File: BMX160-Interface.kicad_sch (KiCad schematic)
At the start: 1 part, among them U1 BMX160

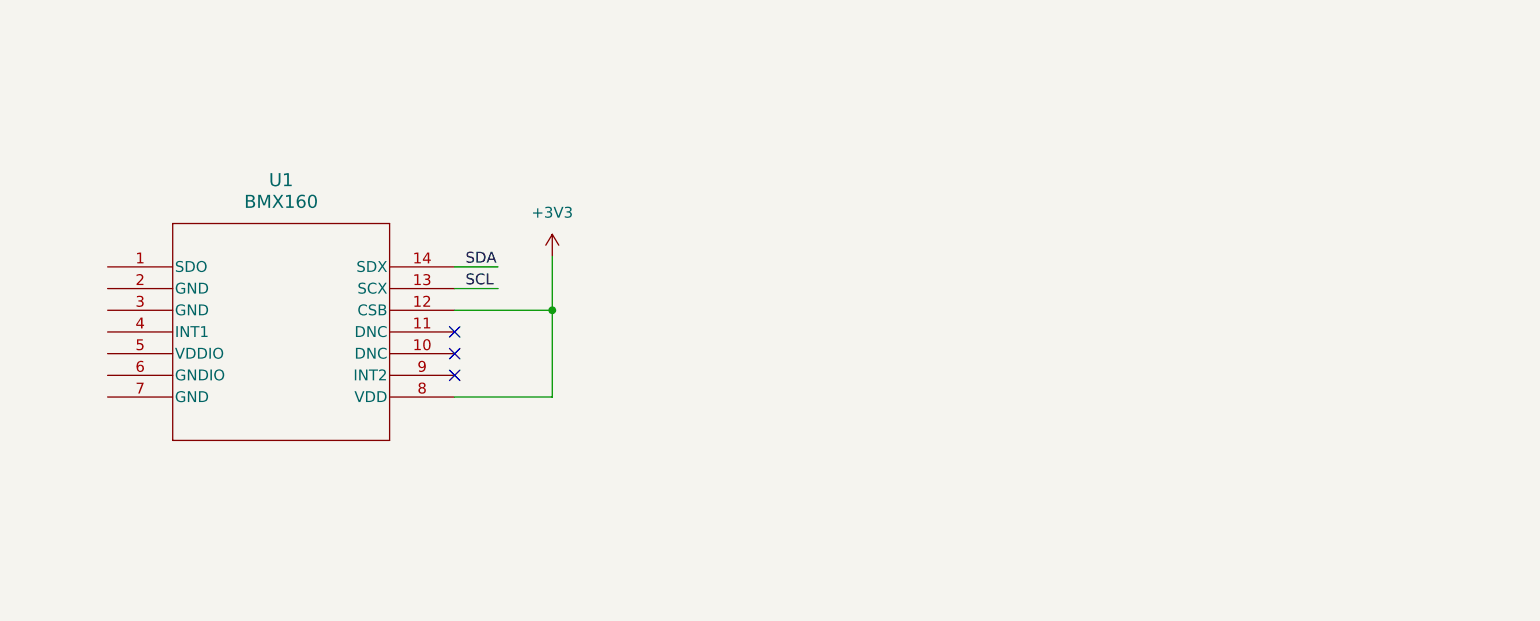
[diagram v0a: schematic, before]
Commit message: Added BMX 160 interface board
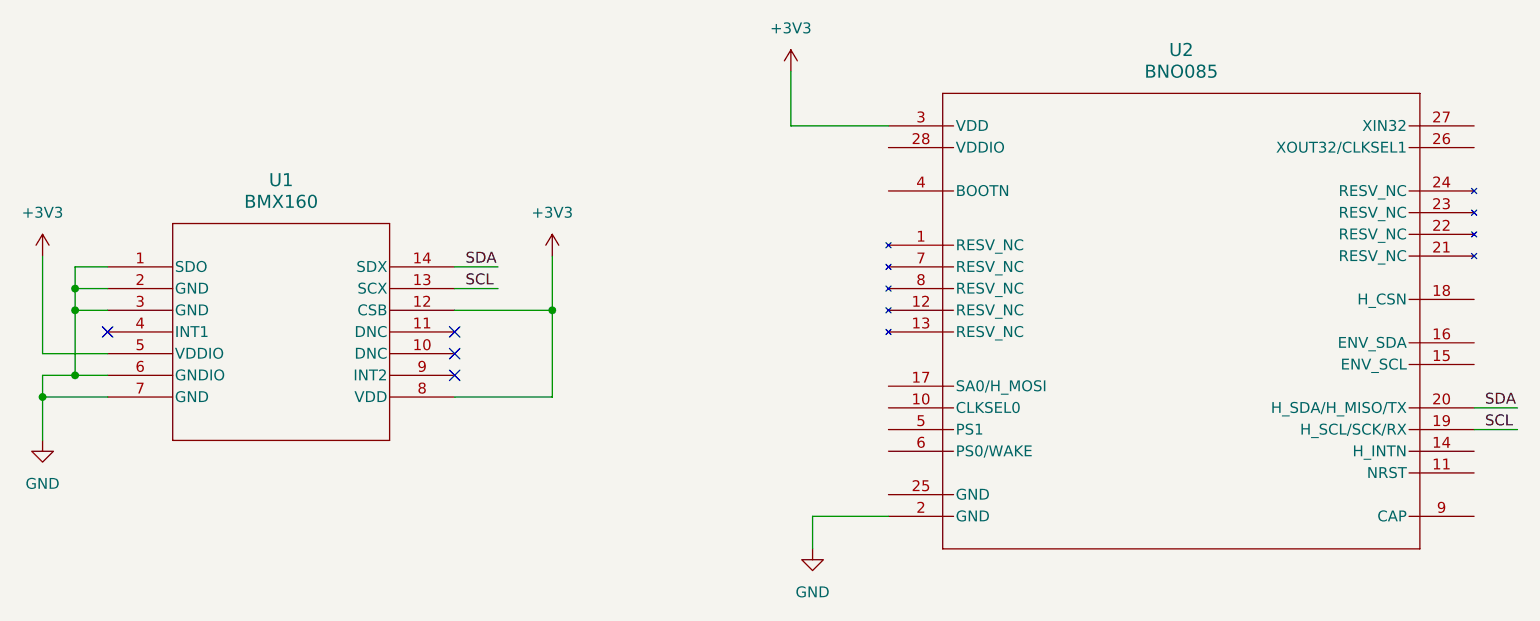
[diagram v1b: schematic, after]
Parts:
- added U2: BNO085, Argus-IC:BNO085_Reversed, symbol Argus-IC:BNO085
- U1: footprint BMX160_BOS -> Argus-IC:BMX160_BOS
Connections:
- net +3V3: now also U1.5 (VDDIO), U2.3 (VDD)
- net SCL: now also U2.19 (H_SCL/SCK/RX)
- net SDA: now also U2.20 (H_SDA/H_MISO/TX)
- net GND: now reaches U1.1 (SDO)
- net GND: now also U1.2 (GND), U1.3 (GND), U1.6 (GNDIO), U1.7 (GND), U2.2 (GND)
- no-connect marks 3 -> 4
